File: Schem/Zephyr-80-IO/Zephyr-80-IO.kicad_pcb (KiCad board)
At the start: 6 copper layers, 160 x 64.4 mm, 90 parts, among them IC1 Z80CTC, IC2 Z80SIO, IC3 Z80SIO, J1 pBITzBus, J2 548190519, J3 L77HDA26SD1CH4F, J5 Conn_01x08_Pin, SW1 SW_Push, SW2 SW_Push, SW3 SW_Coded_SH-7070, SW4 SW_Coded_SH-7070, SW5 SW_Coded_SH-7070, SW6 SW_Coded_SH-7070, U1 74AHCT125, U10 74HC688, U11 74HC688, U12 74HC688, U14 MAX202IDR, U15 PIC18F57Q84-I/PT, U2 74AHCT1G125, U4 74AHC595, U5 74AHC595, U6 74HC138, U7 FT230XS-U, U8 SN74HC4040DR, U9 74HC688, Y1 ECS-2100AX-147.4

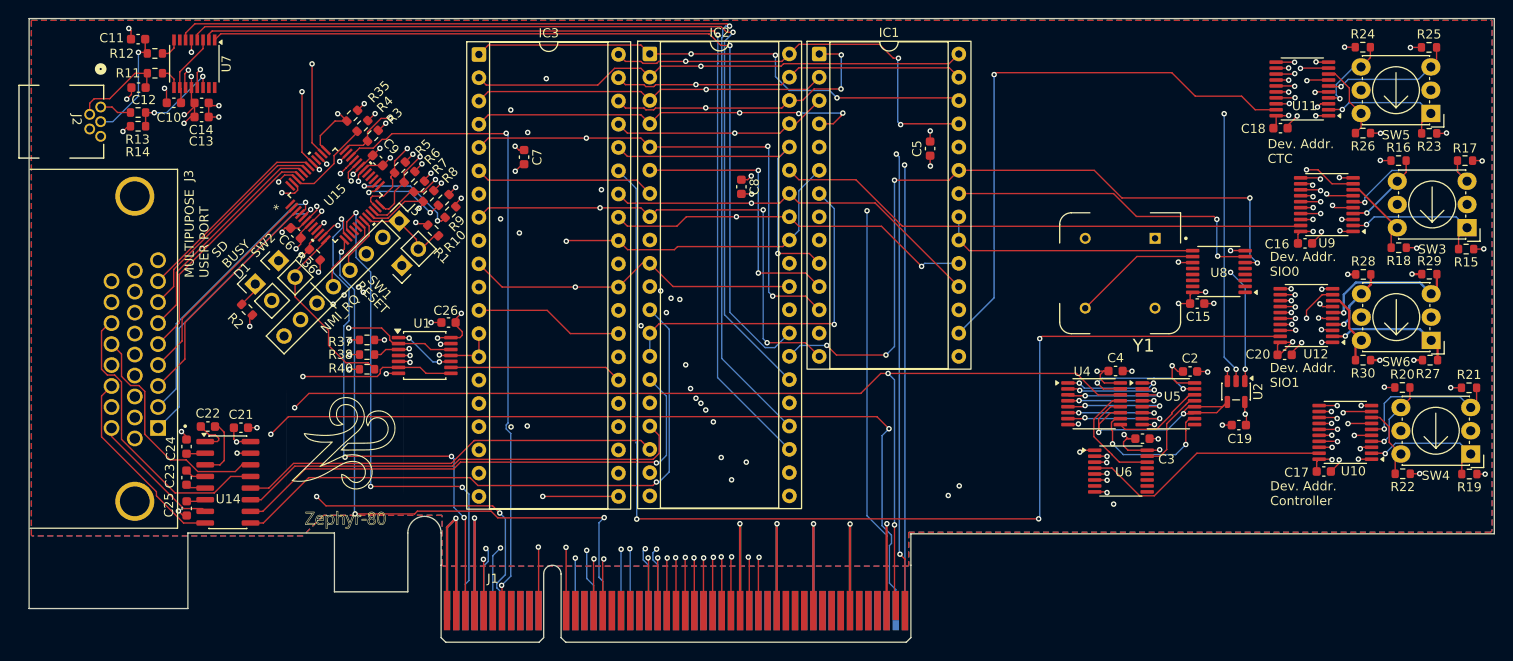
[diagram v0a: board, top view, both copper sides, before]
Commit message: Fixed a few mistakes in the IO Controller
* Wrong layer for vertical traces (should not be on the same layer as vcc plane)
* Added pull-downs for DCD for all SIOs (we don't use this line)
* Connected DCD and CTS to the MCU for SIO1 in case we want to use it to gate the SIO1
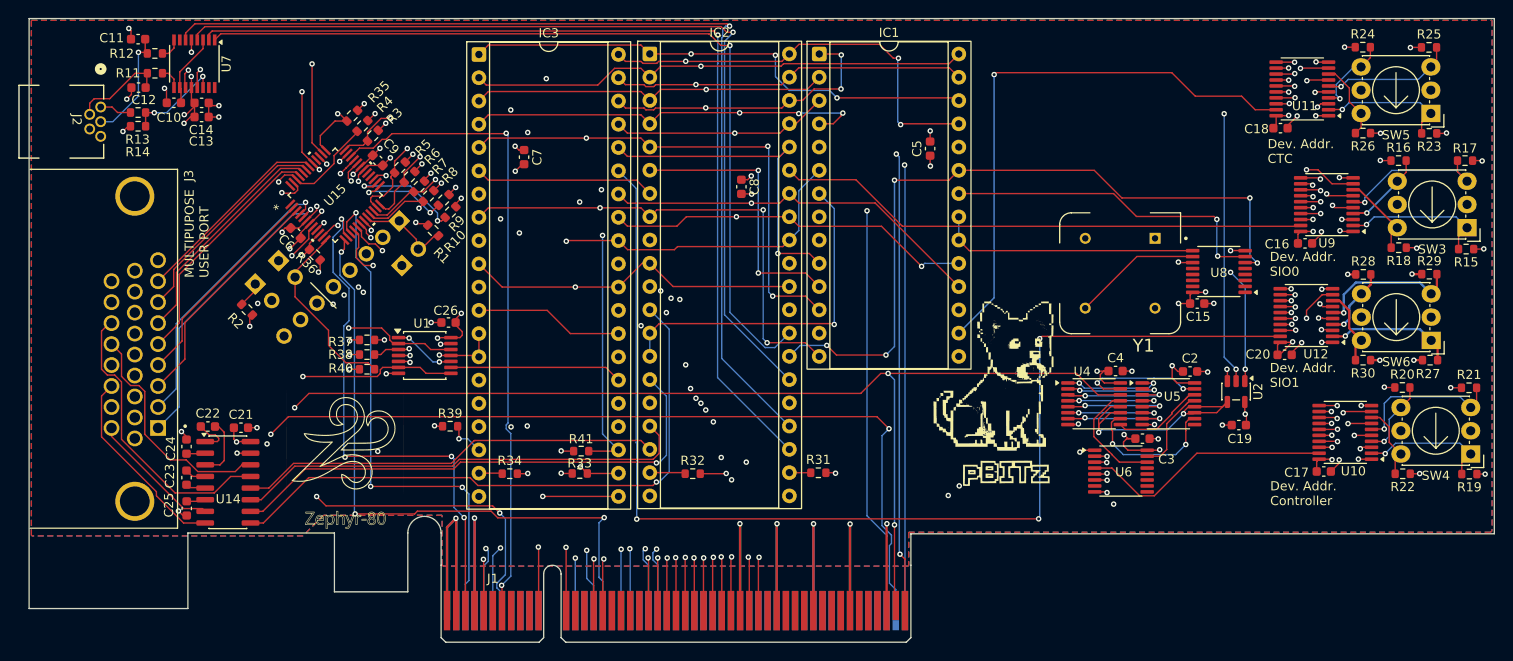
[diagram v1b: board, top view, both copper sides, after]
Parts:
- added R31: 10k, Resistor_SMD:R_0603_1608Metric, F.Cu at (162.7, 100.2)
- added R32: 10k, Resistor_SMD:R_0603_1608Metric, F.Cu at (149.0, 100.3)
- added R33: 10k, Resistor_SMD:R_0603_1608Metric, F.Cu at (136.7, 100.3)
- added R34: 10k, Resistor_SMD:R_0603_1608Metric, F.Cu at (129.0, 100.3)
- added R39: 10k, Resistor_SMD:R_0603_1608Metric, F.Cu at (122.5, 95.2)
- added R41: 10k, Resistor_SMD:R_0603_1608Metric, F.Cu at (136.8, 97.9)
- D1, J5, SW1, SW2: moved to B.Cu
- G***: moved to F.Cu
- moved G*** 71.7 mm to (183.2, 90.3), turned to 0 degrees
- turned D1 to -135 degrees
- turned J5 to 135 degrees
- turned SW1 to -45 degrees
- turned SW2 to -135 degrees
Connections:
- net /Baud Clock/CLK_1M8441 renamed /Baud Clock/CLK_1M8432
- net /Baud Clock/CLK_3M6882 renamed /Baud Clock/CLK_3M6864
- net /Baud Clock/CLK_7M3764 renamed /Baud Clock/CLK_7M3728
- IC2 pad 19: unconnected-(IC2-DCDA-Pad19) -> Net-(IC2-DCDA)
- IC2 pad 22: unconnected-(IC2-DCDB-Pad22) -> Net-(IC2-DCDB)
- IC3 pad 18: unconnected-(IC3-CTSA-Pad18) -> /IO Controller Card/~{CTSA}
- IC3 pad 19: unconnected-(IC3-DCDA-Pad19) -> /IO Controller Card/~{DCDA}
- IC3 pad 22: unconnected-(IC3-DCDB-Pad22) -> /IO Controller Card/~{DCDB}
- IC3 pad 23: unconnected-(IC3-CTSB-Pad23) -> /IO Controller Card/~{CTSB}
- U15 pad 16: unconnected-(U15-RB4-Pad16) -> /IO Controller Card/~{DCDA}
- U15 pad 17: unconnected-(U15-RB5-Pad17) -> /IO Controller Card/~{CTSB}
- U15 pad 27: unconnected-(U15-RE0-Pad27) -> /IO Controller Card/~{DCDB}
- U15 pad 8: unconnected-(U15-RB0-Pad8) -> /IO Controller Card/~{CTSA}
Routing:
- net /IO Controller Card/~{DCDB}: track 0.00 -> 57.5 mm, vias 0 -> 3
- net /IO Controller Card/~{CTSB}: track 0.00 -> 57.1 mm, vias 0 -> 2
- net /IO Controller Card/~{CTSA}: track 0.00 -> 51.9 mm, vias 0 -> 4
- net /IO Controller Card/~{DCDA}: track 0.00 -> 40.6 mm, vias 0 -> 2
- net GND: track 237.0 -> 245.5 mm, vias 85 -> 91
- net Net-(IC2-DCDA): track 0.00 -> 3.91 mm
- net Net-(IC2-DCDB): track 0.00 -> 2.34 mm
- net Net-(J5-Pin_5): track 8.53 -> 10.4 mm, vias 0 -> 1
- net Net-(J5-Pin_4): track 6.59 -> 6.73 mm, vias 0 -> 1
- removed copper zone on In4.Cu, net +5V

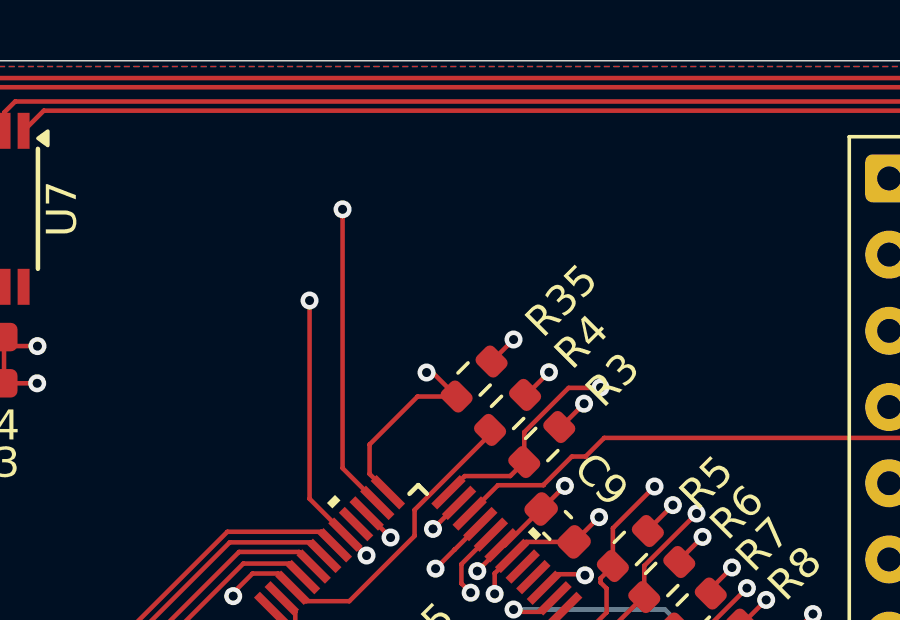
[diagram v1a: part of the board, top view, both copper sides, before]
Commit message: updated the pullups for the power on sequence pins
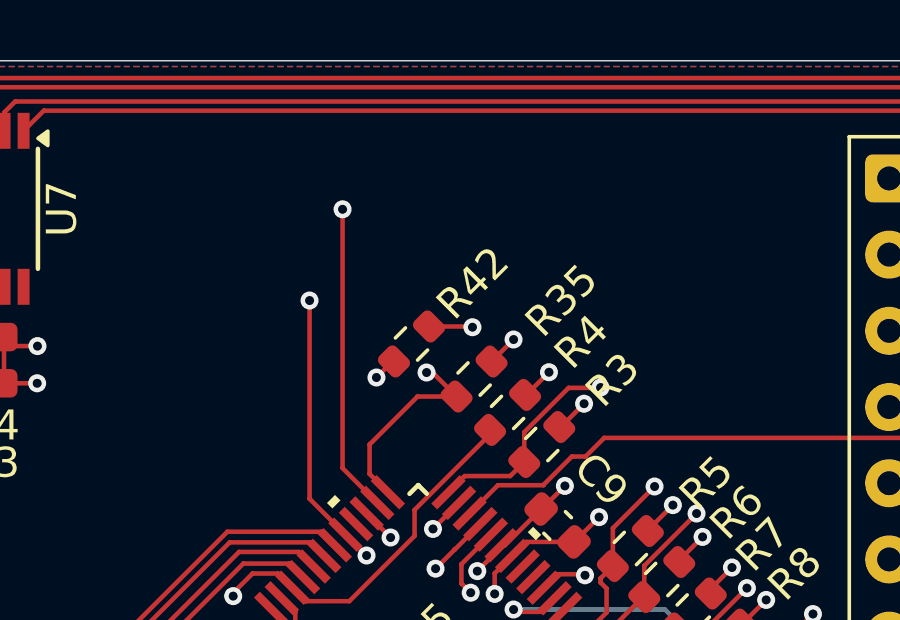
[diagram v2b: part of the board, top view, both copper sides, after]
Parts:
- added R42: 10k, Resistor_SMD:R_0603_1608Metric, F.Cu at (109.7, 60.1)
- R36, R37, R38, R4: value 100k -> 10k
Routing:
- net /IO Controller Card/~{SHUTDOWN_RQ}: track 57.4 -> 72.0 mm, vias 3 -> 4
- net +5V: track 141.4 -> 142.9 mm, vias 56 -> 57

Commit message: Corrections post review
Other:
- board text added: "DNP"
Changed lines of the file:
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@@
 		)
 	)
+	(gr_text "DNP"
+		(at 116.3826 59.8856 45)
+		(layer "F.SilkS")
+		(effects
+			(font
+				(size 1 1)
+				(thickness 0.15)
+			)
+			(justify left bottom)
+		)
+	)
 	(gr_text "MULTIPUPOSE\nUSER PORT"
 		(at 96.2404 78.961 90)
@@
 	)
 	(segment
+		(start 111.217285 72.86413)
+		(end 112.229366 71.852049)
+		(width 0.1524)
+		(layer "F.Cu")
+		(net "/IO Controller Card/~{SHUTDOWN_RQ}")
+	)
+	(segment
+		(start 113.83 101.74)
+		(end 123.73 101.74)
+		(width 0.1524)
+		(layer "F.Cu")
+		(net "/IO Controller Card/~{SHUTDOWN_RQ}")
+	)
+	(segment
+		(start 111.217285 73.672157)
+		(end 111.217285 72.86413)
+		(width 0.1524)
+		(layer "F.Cu")
+		(net "/IO Controller Card/~{SHUTDOWN_RQ}")
+	)
+	(segment
+		(start 109.093637 60.672163)
+		(end 108.5594 61.2064)
+		(width 0.1524)
+		(layer "F.Cu")
+		(net "/IO Controller Card/~{SHUTDOWN_RQ}")
+	)
+	(segment
+		(start 123.73 101.74)
+		(end 123.83 101.84)
+		(width 0.1524)
+		(layer "F.Cu")
+		(net "/IO Controller Card/~{SHUTDOWN_RQ}")
+	)
+	(segment
+		(start 111.667068 74.12194)
+		(end 111.217285 73.672157)
+		(width 0.1524)
+		(layer "F.Cu")
+		(net "/IO Controller Card/~{SHUTDOWN_RQ}")
+	)
+	(segment
+		(start 109.144437 60.672163)
+		(end 109.093637 60.672163)
+		(width 0.1524)
+		(layer "F.Cu")
+		(net "/IO Controller Card/~{SHUTDOWN_RQ}")
+	)
+	(via
+		(at 112.229366 71.852049)
+		(size 0.6)
+		(drill 0.3)
+		(layers "F.Cu" "B.Cu")
+		(net "/IO Controller Card/~{SHUTDOWN_RQ}")
+	)
+	(via
+		(at 113.83 101.74)
+		(size 0.6)
+		(drill 0.3)
+		(layers "F.Cu" "B.Cu")
+		(net "/IO Controller Card/~{SHUTDOWN_RQ}")
+	)
+	(via
+		(at 123.83 101.84)
+		(size 0.6)
+		(drill 0.3)
+		(layers "F.Cu" "B.Cu")
+		(net "/IO Controller Card/~{SHUTDOWN_RQ}")
+	)
+	(via
+		(at 108.5594 61.2064)
+		(size 0.6)
+		(drill 0.3)
+		(layers "F.Cu" "B.Cu")
+		(net "/IO Controller Card/~{SHUTDOWN_RQ}")
+	)
+	(segment
+		(start 124.17 112.4)
+		(end 124.17 115.3)
+		(width 0.1524)
+		(layer "B.Cu")
+		(net "/IO Controller Card/~{SHUTDOWN_RQ}")
+	)
+	(segment
+		(start 112.229366 76.735788)
+		(end 113.83 78.336422)
+		(width 0.1524)
+		(layer "B.Cu")
+		(net "/IO Controller Card/~{SHUTDOWN_RQ}")
+	)
+	(segment
+		(start 123.83 101.84)
+		(end 124.5586 102.5686)
+		(width 0.1524)
+		(layer "B.Cu")
+		(net "/IO Controller Card/~{SHUTDOWN_RQ}")
+	)
+	(segment
+		(start 113.83 78.336422)
+		(end 113.83 101.74)
+		(width 0.1524)
+		(layer "B.Cu")
+		(net "/IO Controller Card/~{SHUTDOWN_RQ}")
+	)
+	(segment
+		(start 112.229366 71.852049)
+		(end 112.229366 76.735788)
+		(width 0.1524)
+		(layer "B.Cu")
+		(net "/IO Controller Card/~{SHUTDOWN_RQ}")
+	)
+	(segment
+		(start 124.5586 112.0114)
+		(end 124.17 112.4)
+		(width 0.1524)
+		(layer "B.Cu")
+		(net "/IO Controller Card/~{SHUTDOWN_RQ}")
+	)
+	(segment
+		(start 124.5586 102.5686)
+		(end 124.5586 112.0114)
+		(width 0.1524)
+		(layer "B.Cu")
+		(net "/IO Controller Card/~{SHUTDOWN_RQ}")
+	)
+	(segment
+		(start 114.1586 66.8056)
+		(end 114.1586 69.922815)
+		(width 0.1524)
+		(layer "In4.Cu")
+		(net "/IO Controller Card/~{SHUTDOWN_RQ}")
+	)
+	(segment
+		(start 108.5594 61.2064)
+		(end 114.1586 66.8056)
+		(width 0.1524)
+		(layer "In4.Cu")
+		(net "/IO Controller Card/~{SHUTDOWN_RQ}")
+	)
+	(segment
+		(start 114.1586 69.922815)
+		(end 112.229366 71.852049)
+		(width 0.1524)
+		(layer "In4.Cu")
+		(net "/IO Controller Card/~{SHUTDOWN_RQ}")
+	)
+	(segment
 		(start 116.8675 85.49)
 		(end 117.98 85.49)
@@
 	)
 	(segment
-		(start 111.217285 72.86413)
-		(end 112.229366 71.852049)
-		(width 0.1524)
-		(layer "F.Cu")
-		(net "/IO Controller Card/~{SHUTDOWN_RQ}")
-	)
-	(segment
-		(start 113.83 101.74)
-		(end 123.73 101.74)
-		(width 0.1524)
-		(layer "F.Cu")
-		(net "/IO Controller Card/~{SHUTDOWN_RQ}")
-	)
-	(segment
-		(start 111.217285 73.672157)
-		(end 111.217285 72.86413)
-		(width 0.1524)
-		(layer "F.Cu")
-		(net "/IO Controller Card/~{SHUTDOWN_RQ}")
-	)
-	(segment
-		(start 109.093637 60.672163)
-		(end 108.5594 61.2064)
-		(width 0.1524)
-		(layer "F.Cu")
-		(net "/IO Controller Card/~{SHUTDOWN_RQ}")
-	)
-	(segment
-		(start 123.73 101.74)
-		(end 123.83 101.84)
-		(width 0.1524)
-		(layer "F.Cu")
-		(net "/IO Controller Card/~{SHUTDOWN_RQ}")
-	)
-	(segment
-		(start 111.667068 74.12194)
-		(end 111.217285 73.672157)
-		(width 0.1524)
-		(layer "F.Cu")
-		(net "/IO Controller Card/~{SHUTDOWN_RQ}")
-	)
-	(segment
-		(start 109.144437 60.672163)
-		(end 109.093637 60.672163)
-		(width 0.1524)
-		(layer "F.Cu")
-		(net "/IO Controller Card/~{SHUTDOWN_RQ}")
-	)
-	(via
-		(at 112.229366 71.852049)
-		(size 0.6)
-		(drill 0.3)
-		(layers "F.Cu" "B.Cu")
-		(net "/IO Controller Card/~{SHUTDOWN_RQ}")
-	)
-	(via
-		(at 113.83 101.74)
-		(size 0.6)
-		(drill 0.3)
-		(layers "F.Cu" "B.Cu")
-		(net "/IO Controller Card/~{SHUTDOWN_RQ}")
-	)
-	(via
-		(at 123.83 101.84)
-		(size 0.6)
-		(drill 0.3)
-		(layers "F.Cu" "B.Cu")
-		(net "/IO Controller Card/~{SHUTDOWN_RQ}")
-	)
-	(via
-		(at 108.5594 61.2064)
-		(size 0.6)
-		(drill 0.3)
-		(layers "F.Cu" "B.Cu")
-		(net "/IO Controller Card/~{SHUTDOWN_RQ}")
-	)
-	(segment
-		(start 124.17 112.4)
-		(end 124.17 115.3)
-		(width 0.1524)
-		(layer "B.Cu")
-		(net "/IO Controller Card/~{SHUTDOWN_RQ}")
-	)
-	(segment
-		(start 112.229366 76.735788)
-		(end 113.83 78.336422)
-		(width 0.1524)
-		(layer "B.Cu")
-		(net "/IO Controller Card/~{SHUTDOWN_RQ}")
-	)
-	(segment
-		(start 123.83 101.84)
-		(end 124.5586 102.5686)
-		(width 0.1524)
-		(layer "B.Cu")
-		(net "/IO Controller Card/~{SHUTDOWN_RQ}")
-	)
-	(segment
-		(start 113.83 78.336422)
-		(end 113.83 101.74)
-		(width 0.1524)
-		(layer "B.Cu")
-		(net "/IO Controller Card/~{SHUTDOWN_RQ}")
-	)
-	(segment
-		(start 112.229366 71.852049)
-		(end 112.229366 76.735788)
-		(width 0.1524)
-		(layer "B.Cu")
-		(net "/IO Controller Card/~{SHUTDOWN_RQ}")
-	)
-	(segment
-		(start 124.5586 112.0114)
-		(end 124.17 112.4)
-		(width 0.1524)
-		(layer "B.Cu")
-		(net "/IO Controller Card/~{SHUTDOWN_RQ}")
-	)
-	(segment
-		(start 124.5586 102.5686)
-		(end 124.5586 112.0114)
-		(width 0.1524)
-		(layer "B.Cu")
-		(net "/IO Controller Card/~{SHUTDOWN_RQ}")
-	)
-	(segment
-		(start 114.1586 66.8056)
-		(end 114.1586 69.922815)
-		(width 0.1524)
-		(layer "In4.Cu")
-		(net "/IO Controller Card/~{SHUTDOWN_RQ}")
-	)
-	(segment
-		(start 108.5594 61.2064)
-		(end 114.1586 66.8056)
-		(width 0.1524)
-		(layer "In4.Cu")
-		(net "/IO Controller Card/~{SHUTDOWN_RQ}")
-	)
-	(segment
-		(start 114.1586 69.922815)
-		(end 112.229366 71.852049)
-		(width 0.1524)
-		(layer "In4.Cu")
-		(net "/IO Controller Card/~{SHUTDOWN_RQ}")
-	)
-	(segment
